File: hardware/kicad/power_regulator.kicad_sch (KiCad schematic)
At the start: 4 parts, among them U4 XC6220

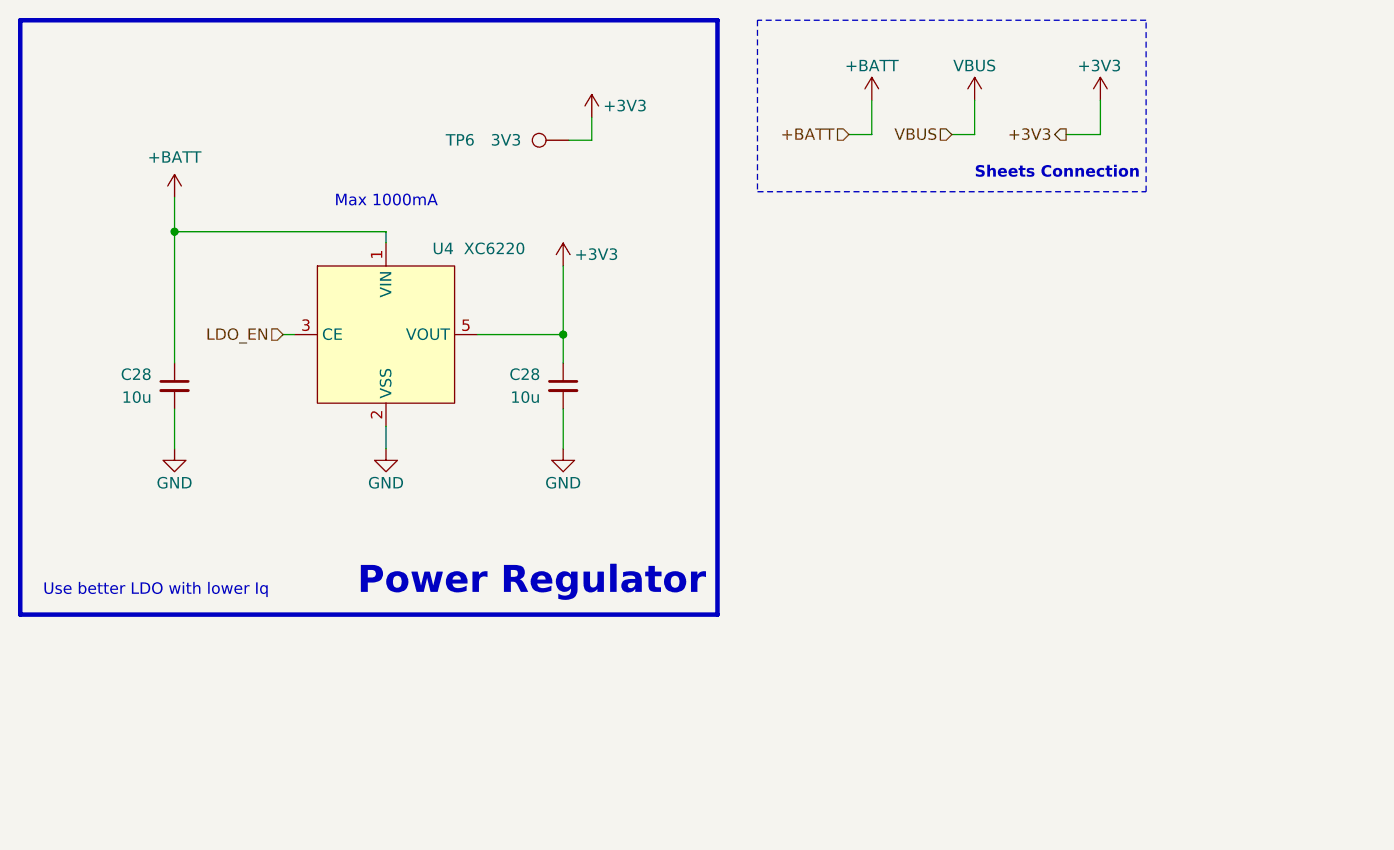
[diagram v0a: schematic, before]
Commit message: re-route sense out, add display power switch
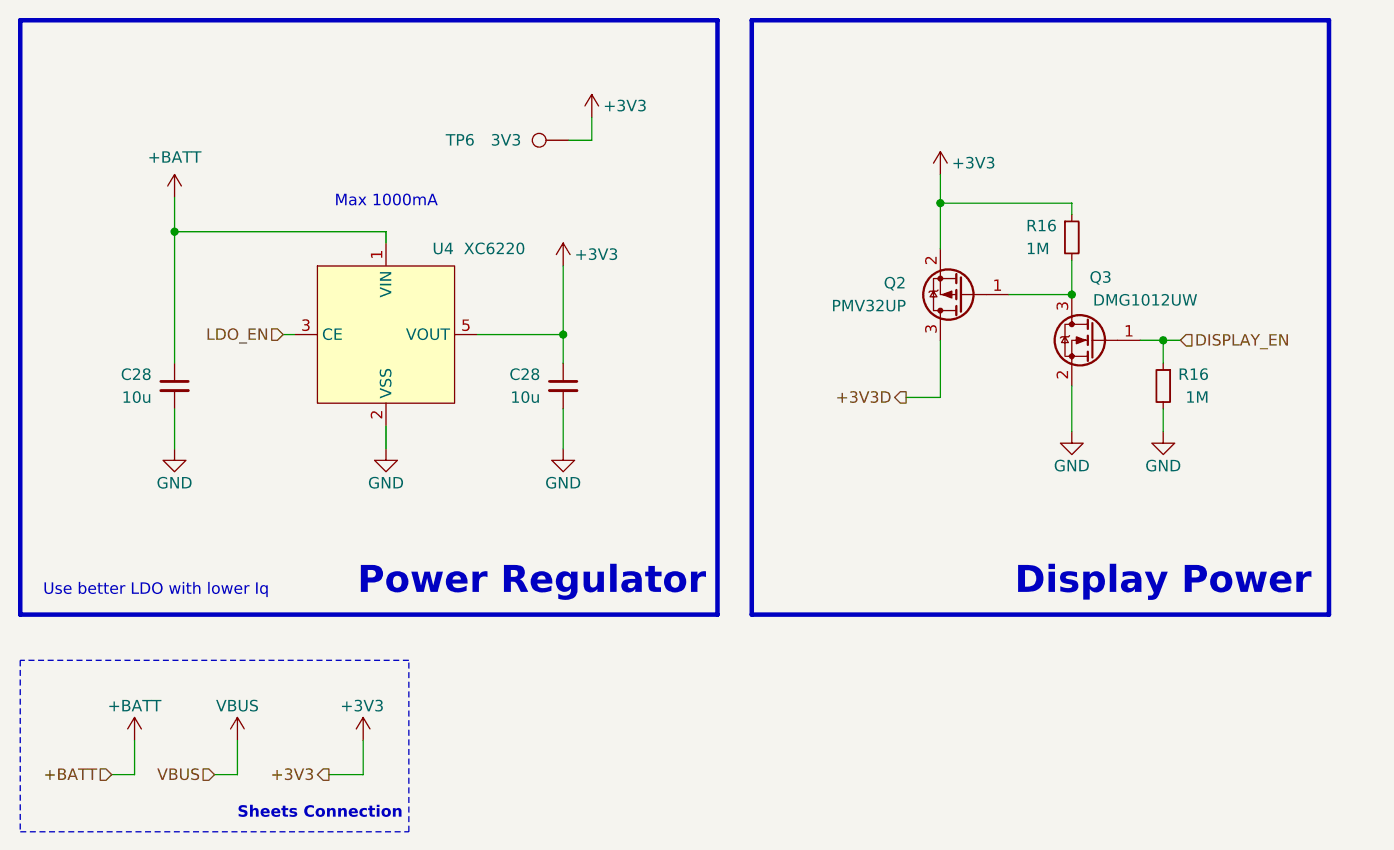
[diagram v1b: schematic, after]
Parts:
- added Q2: PMV32UP, Package_TO_SOT_SMD:SOT-23, symbol Device:Q_PMOS_GSD
- added Q3: DMG1012UW, Package_TO_SOT_SMD:SOT-323_SC-70, symbol Device:Q_NMOS_GSD
- added R16 (x2): 1M, Resistor_SMD:R_0402_1005Metric, symbol Device:R_Small
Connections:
- net +3V3: now also Q2.2 (S), R16.1
- net GND: now also Q3.2 (S), R16.2
- new net: Q2.1 (G), Q3.3 (D), R16.2
- new net +3V3D: Q2.3 (D)
- new net DISPLAY_EN: Q3.1 (G), R16.1
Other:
- note added: "Display Power"

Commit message: revision 3 prod
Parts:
- added C28: 10u, Capacitor_SMD:C_0603_1608Metric, symbol Device:C_Small
- added TP6: 3V3D, TestPoint:TestPoint_Pad_D1.0mm, symbol Connector:TestPoint
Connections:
- net +3V3D: now also C28.1, TP6.1
- net GND: now also C28.2

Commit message: fix schematic info
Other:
- company: (none) -> Teapot Laboratories
- title: (none) -> Power Regulator
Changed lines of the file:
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@@
   (paper "A4")
   (title_block
-    (date "2023-10-16")
-    (rev "2")
+    (title "Power Regulator")
+    (date "2024-01-10")
+    (rev "3")
+    (company "Teapot Laboratories")
   )
   (junction (at 220.98 95.885) (diameter 0) (color 0 0 0 0)

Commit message: update bom
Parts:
- renumbered C28 to C24, C28 to C25, C28 to C26, Q2 to Q8, Q3 to Q9, R16 to R28, R16 to R29, TP6 to TP10, TP6 to TP5, U4 to U6
